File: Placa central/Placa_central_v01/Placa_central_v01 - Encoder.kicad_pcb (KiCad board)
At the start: 2 copper layers, 20 parts, among them J1 Conn_01x01_Female, J2 Conn_01x01_Female, J3 Conn_01x01_Female, J4 Conn_01x01_Female, J5 Conn_01x01_Female, J6 Conn_01x01_Female, U1 TCRT5000Esq, U2 LM741Esq, U3 TCRT5000Dir, U4 LM741

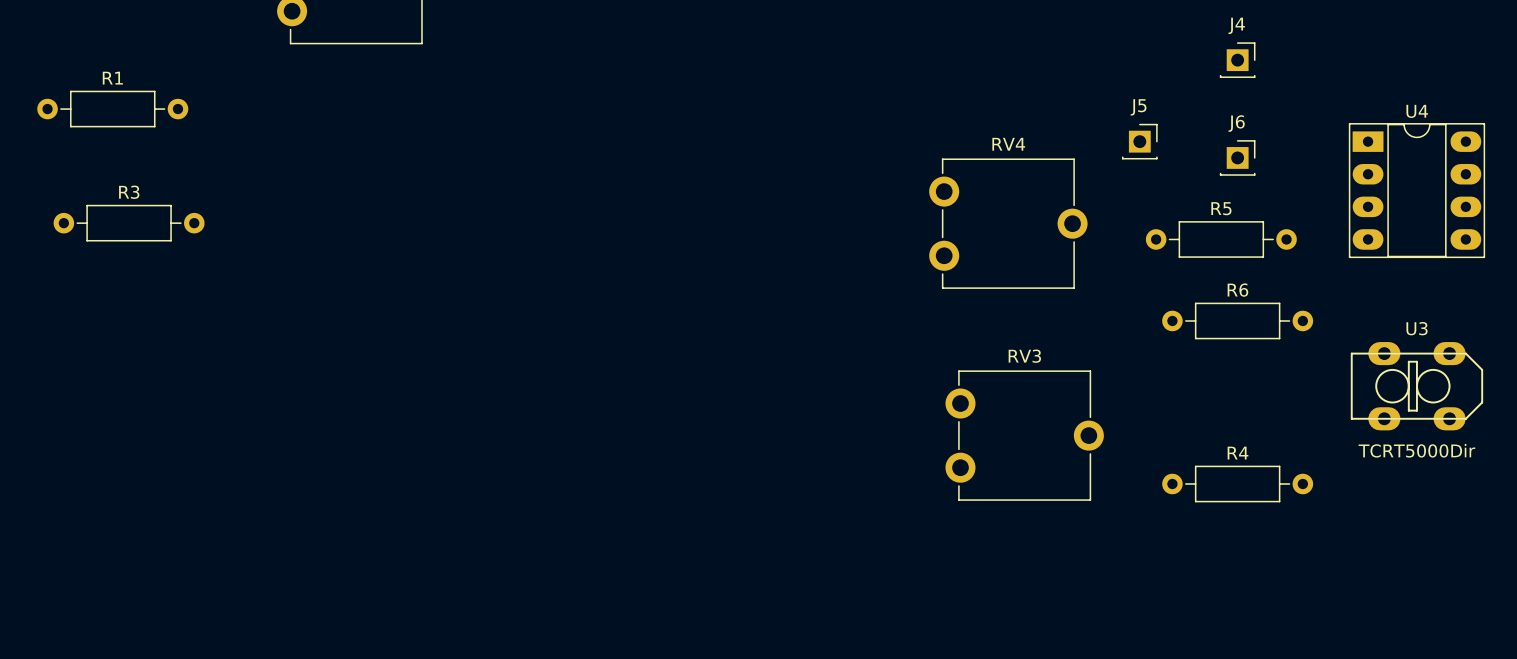
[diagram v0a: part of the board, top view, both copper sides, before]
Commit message: Adicionado Furos a placa encoder. Falta root
Adicionados os furos do suporte para o andar superior e para fixação no case do motor. Falta root
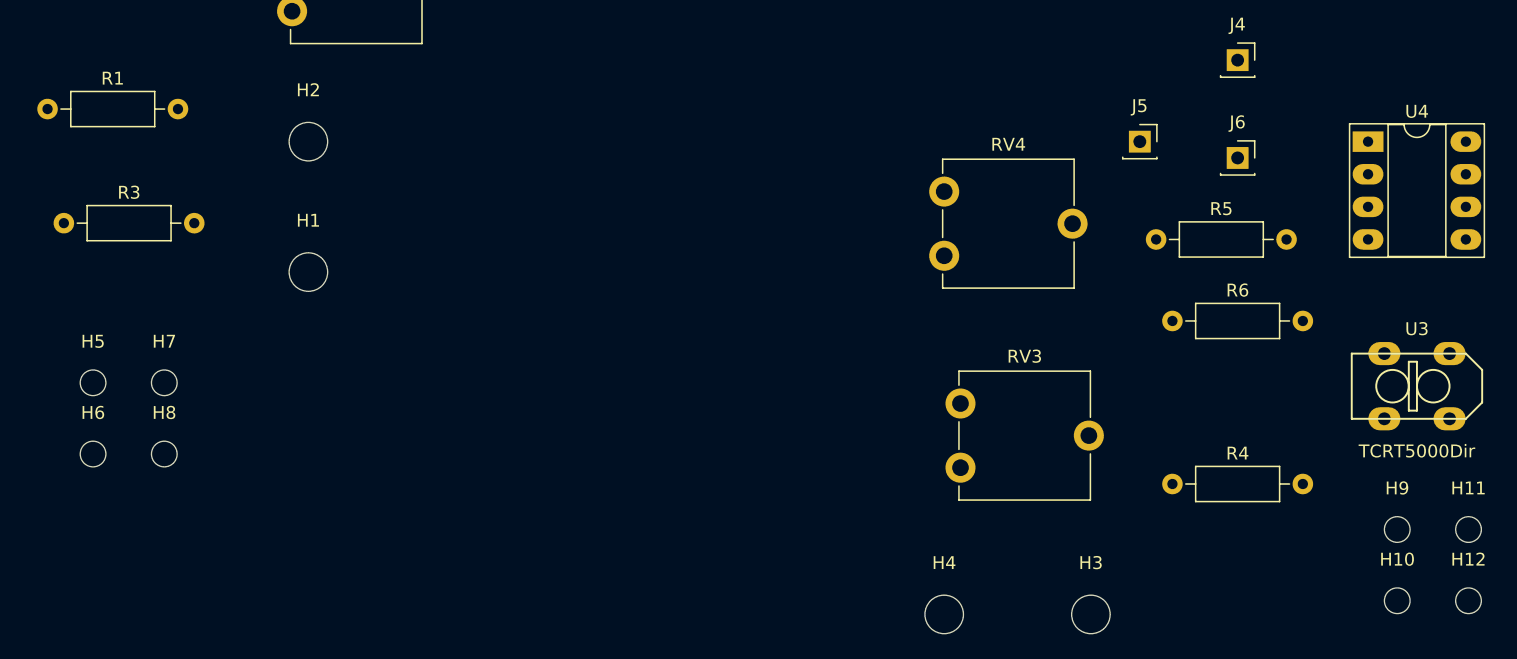
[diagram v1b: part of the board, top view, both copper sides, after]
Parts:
- added H1: Furo1Esq, MountingHole:MountingHole_3mm, F.Cu at (130.8, 110.5)
- added H10: Furo4Dir, MountingHole:MountingHole_2mm, F.Cu at (215.6, 136.1)
- added H11: Furo5Dir, MountingHole:MountingHole_2mm, F.Cu at (221.2, 130.5)
- added H12: Furo6Dir, MountingHole:MountingHole_2mm, F.Cu at (221.2, 136.1)
- added H2: Furo2Esq, MountingHole:MountingHole_3mm, F.Cu at (130.8, 100.3)
- added H3: Furo1Dir, MountingHole:MountingHole_3mm, F.Cu at (191.8, 137.2)
- added H4: Furo2Dir, MountingHole:MountingHole_3mm, F.Cu at (180.3, 137.2)
- added H5: Furo3Esq, MountingHole:MountingHole_2mm, F.Cu at (114.0, 119.1)
- added H6: Furo4Esq, MountingHole:MountingHole_2mm, F.Cu at (114.0, 124.7)
- added H7: Furo5Esq, MountingHole:MountingHole_2mm, F.Cu at (119.6, 119.1)
- added H8: Furo6Esq, MountingHole:MountingHole_2mm, F.Cu at (119.6, 124.7)
- added H9: Furo3Dir, MountingHole:MountingHole_2mm, F.Cu at (215.6, 130.5)
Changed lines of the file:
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@@
     (tracks 0)
     (zones 0)
-    (modules 20)
+    (modules 32)
     (nets 27)
   )
@@
     )
   )
+  (module MountingHole:MountingHole_3mm (layer F.Cu)
+    (at 130.81 110.49)
+    (descr "Mounting Hole 3mm, no annular")
+    (tags "mounting hole 3mm no annular")
+    (attr virtual)
+    (fp_text reference H1 (at 0 -4) (layer F.SilkS)
+      (effects (font (size 1 1) (thickness 0.15)))
+    )
+    (fp_text value Furo1Esq (at 0 4) (layer F.Fab)
+      (effects (font (size 1 1) (thickness 0.15)))
+    )
+    (fp_text user %R (at 0.3 0) (layer F.Fab)
+      (effects (font (size 1 1) (thickness 0.15)))
+    )
+    (fp_circle (center 0 0) (end 3 0) (layer Cmts.User) (width 0.15))
+    (fp_circle (center 0 0) (end 3.25 0) (layer F.CrtYd) (width 0.05))
+    (pad 1 np_thru_hole circle (at 0 0) (size 3 3) (drill 3) (layers *.Cu *.Mask))
+  )
+  (module MountingHole:MountingHole_3mm (layer F.Cu)
+    (at 130.81 100.33)
+    (descr "Mounting Hole 3mm, no annular")
+    (tags "mounting hole 3mm no annular")
+    (attr virtual)
+    (fp_text reference H2 (at 0 -4) (layer F.SilkS)
+      (effects (font (size 1 1) (thickness 0.15)))
+    )
+    (fp_text value Furo2Esq (at 0 4) (layer F.Fab)
+      (effects (font (size 1 1) (thickness 0.15)))
+    )
+    (fp_circle (center 0 0) (end 3.25 0) (layer F.CrtYd) (width 0.05))
+    (fp_circle (center 0 0) (end 3 0) (layer Cmts.User) (width 0.15))
+    (fp_text user %R (at 0.3 0) (layer F.Fab)
+      (effects (font (size 1 1) (thickness 0.15)))
+    )
+    (pad 1 np_thru_hole circle (at 0 0) (size 3 3) (drill 3) (layers *.Cu *.Mask))
+  )
+  (module MountingHole:MountingHole_3mm (layer F.Cu)
+    (at 191.77 137.16)
+    (descr "Mounting Hole 3mm, no annular")
+    (tags "mounting hole 3mm no annular")
+    (attr virtual)
+    (fp_text reference H3 (at 0 -4) (layer F.SilkS)
+      (effects (font (size 1 1) (thickness 0.15)))
+    )
+    (fp_text value Furo1Dir (at 0 4) (layer F.Fab)
+      (effects (font (size 1 1) (thickness 0.15)))
+    )
+    (fp_text user %R (at 0.3 0) (layer F.Fab)
+      (effects (font (size 1 1) (thickness 0.15)))
+    )
+    (fp_circle (center 0 0) (end 3 0) (layer Cmts.User) (width 0.15))
+    (fp_circle (center 0 0) (end 3.25 0) (layer F.CrtYd) (width 0.05))
+    (pad 1 np_thru_hole circle (at 0 0) (size 3 3) (drill 3) (layers *.Cu *.Mask))
+  )
+  (module MountingHole:MountingHole_3mm (layer F.Cu)
+    (at 180.34 137.16)
+    (descr "Mounting Hole 3mm, no annular")
+    (tags "mounting hole 3mm no annular")
+    (attr virtual)
+    (fp_text reference H4 (at 0 -4) (layer F.SilkS)
+      (effects (font (size 1 1) (thickness 0.15)))
+    )
+    (fp_text value Furo2Dir (at 0 4) (layer F.Fab)
+      (effects (font (size 1 1) (thickness 0.15)))
+    )
+    (fp_circle (center 0 0) (end 3.25 0) (layer F.CrtYd) (width 0.05))
+    (fp_circle (center 0 0) (end 3 0) (layer Cmts.User) (width 0.15))
+    (fp_text user %R (at 0.3 0) (layer F.Fab)
+      (effects (font (size 1 1) (thickness 0.15)))
+    )
+    (pad 1 np_thru_hole circle (at 0 0) (size 3 3) (drill 3) (layers *.Cu *.Mask))
+  )
+  (module MountingHole:MountingHole_2mm (layer F.Cu)
+    (at 114.035001 119.115001)
+    (descr "Mounting Hole 2mm, no annular")
+    (tags "mounting hole 2mm no annular")
+    (attr virtual)
+    (fp_text reference H5 (at 0 -3.2) (layer F.SilkS)
+      (effects (font (size 1 1) (thickness 0.15)))
+    )
+    (fp_text value Furo3Esq (at 0 3.1) (layer F.Fab)
+      (effects (font (size 1 1) (thickness 0.15)))
+    )
+    (fp_circle (center 0 0) (end 2.25 0) (layer F.CrtYd) (width 0.05))
+    (fp_circle (center 0 0) (end 2 0) (layer Cmts.User) (width 0.15))
+    (fp_text user %R (at 0.3 0) (layer F.Fab)
+      (effects (font (size 1 1) (thickness 0.15)))
+    )
+    (pad "" np_thru_hole circle (at 0 0) (size 2 2) (drill 2) (layers *.Cu *.Mask))
+  )
+  (module MountingHole:MountingHole_2mm (layer F.Cu)
+    (at 114.035001 124.665001)
+    (descr "Mounting Hole 2mm, no annular")
+    (tags "mounting hole 2mm no annular")
+    (attr virtual)
+    (fp_text reference H6 (at 0 -3.2) (layer F.SilkS)
+      (effects (font (size 1 1) (thickness 0.15)))
+    )
+    (fp_text value Furo4Esq (at 0 3.1) (layer F.Fab)
+      (effects (font (size 1 1) (thickness 0.15)))
+    )
+    (fp_text user %R (at 0.3 0) (layer F.Fab)
+      (effects (font (size 1 1) (thickness 0.15)))
+    )
+    (fp_circle (center 0 0) (end 2 0) (layer Cmts.User) (width 0.15))
+    (fp_circle (center 0 0) (end 2.25 0) (layer F.CrtYd) (width 0.05))
+    (pad "" np_thru_hole circle (at 0 0) (size 2 2) (drill 2) (layers *.Cu *.Mask))
+  )
+  (module MountingHole:MountingHole_2mm (layer F.Cu)
+    (at 119.585001 119.115001)
+    (descr "Mounting Hole 2mm, no annular")
+    (tags "mounting hole 2mm no annular")
+    (attr virtual)
+    (fp_text reference H7 (at 0 -3.2) (layer F.SilkS)
+      (effects (font (size 1 1) (thickness 0.15)))
+    )
+    (fp_text value Furo5Esq (at 0 3.1) (layer F.Fab)
+      (effects (font (size 1 1) (thickness 0.15)))
+    )
+    (fp_text user %R (at 0.3 0) (layer F.Fab)
+      (effects (font (size 1 1) (thickness 0.15)))
+    )
+    (fp_circle (center 0 0) (end 2 0) (layer Cmts.User) (width 0.15))
+    (fp_circle (center 0 0) (end 2.25 0) (layer F.CrtYd) (width 0.05))
+    (pad "" np_thru_hole circle (at 0 0) (size 2 2) (drill 2) (layers *.Cu *.Mask))
+  )
+  (module MountingHole:MountingHole_2mm (layer F.Cu)
+    (at 119.585001 124.665001)
+    (descr "Mounting Hole 2mm, no annular")
+    (tags "mounting hole 2mm no annular")
+    (attr virtual)
+    (fp_text reference H8 (at 0 -3.2) (layer F.SilkS)
+      (effects (font (size 1 1) (thickness 0.15)))
+    )
+    (fp_text value Furo6Esq (at 0 3.1) (layer F.Fab)
+      (effects (font (size 1 1) (thickness 0.15)))
+    )
+    (fp_circle (center 0 0) (end 2.25 0) (layer F.CrtYd) (width 0.05))
+    (fp_circle (center 0 0) (end 2 0) (layer Cmts.User) (width 0.15))
+    (fp_text user %R (at 0.3 0) (layer F.Fab)
+      (effects (font (size 1 1) (thickness 0.15)))
+    )
+    (pad "" np_thru_hole circle (at 0 0) (size 2 2) (drill 2) (layers *.Cu *.Mask))
+  )
+  (module MountingHole:MountingHole_2mm (layer F.Cu)
+    (at 215.635001 130.545001)
+    (descr "Mounting Hole 2mm, no annular")
+    (tags "mounting hole 2mm no annular")
+    (attr virtual)
+    (fp_text reference H9 (at 0 -3.2) (layer F.SilkS)
+      (effects (font (size 1 1) (thickness 0.15)))
+    )
+    (fp_text value Furo3Dir (at 0 3.1) (layer F.Fab)
+      (effects (font (size 1 1) (thickness 0.15)))
+    )
+    (fp_text user %R (at 0.3 0) (layer F.Fab)
+      (effects (font (size 1 1) (thickness 0.15)))
+    )
+    (fp_circle (center 0 0) (end 2 0) (layer Cmts.User) (width 0.15))
+    (fp_circle (center 0 0) (end 2.25 0) (layer F.CrtYd) (width 0.05))
+    (pad "" np_thru_hole circle (at 0 0) (size 2 2) (drill 2) (layers *.Cu *.Mask))
+  )
+  (module MountingHole:MountingHole_2mm (layer F.Cu)
+    (at 215.635001 136.095001)
+    (descr "Mounting Hole 2mm, no annular")
+    (tags "mounting hole 2mm no annular")
+    (attr virtual)
+    (fp_text reference H10 (at 0 -3.2) (layer F.SilkS)
+      (effects (font (size 1 1) (thickness 0.15)))
+    )
+    (fp_text value Furo4Dir (at 0 3.1) (layer F.Fab)
+      (effects (font (size 1 1) (thickness 0.15)))
+    )
+    (fp_text user %R (at 0.3 0) (layer F.Fab)
+      (effects (font (size 1 1) (thickness 0.15)))
+    )
+    (fp_circle (center 0 0) (end 2 0) (layer Cmts.User) (width 0.15))
+    (fp_circle (center 0 0) (end 2.25 0) (layer F.CrtYd) (width 0.05))
+    (pad "" np_thru_hole circle (at 0 0) (size 2 2) (drill 2) (layers *.Cu *.Mask))
+  )
+  (module MountingHole:MountingHole_2mm (layer F.Cu)
+    (at 221.185001 130.545001)
+    (descr "Mounting Hole 2mm, no annular")
+    (tags "mounting hole 2mm no annular")
+    (attr virtual)
+    (fp_text reference H11 (at 0 -3.2) (layer F.SilkS)
+      (effects (font (size 1 1) (thickness 0.15)))
+    )
+    (fp_text value Furo5Dir (at 0 3.1) (layer F.Fab)
+      (effects (font (size 1 1) (thickness 0.15)))
+    )
+    (fp_circle (center 0 0) (end 2.25 0) (layer F.CrtYd) (width 0.05))
+    (fp_circle (center 0 0) (end 2 0) (layer Cmts.User) (width 0.15))
+    (fp_text user %R (at 0.3 0) (layer F.Fab)
+      (effects (font (size 1 1) (thickness 0.15)))
+    )
+    (pad "" np_thru_hole circle (at 0 0) (size 2 2) (drill 2) (layers *.Cu *.Mask))
+  )
+  (module MountingHole:MountingHole_2mm (layer F.Cu)
+    (at 221.185001 136.095001)
+    (descr "Mounting Hole 2mm, no annular")
+    (tags "mounting hole 2mm no annular")
+    (attr virtual)
+    (fp_text reference H12 (at 0 -3.2) (layer F.SilkS)
+      (effects (font (size 1 1) (thickness 0.15)))
+    )
+    (fp_text value Furo6Dir (at 0 3.1) (layer F.Fab)
+      (effects (font (size 1 1) (thickness 0.15)))
+    )
+    (fp_circle (center 0 0) (end 2.25 0) (layer F.CrtYd) (width 0.05))
+    (fp_circle (center 0 0) (end 2 0) (layer Cmts.User) (width 0.15))
+    (fp_text user %R (at 0.3 0) (layer F.Fab)
+      (effects (font (size 1 1) (thickness 0.15)))
+    )
+    (pad "" np_thru_hole circle (at 0 0) (size 2 2) (drill 2) (layers *.Cu *.Mask))
+  )
 )

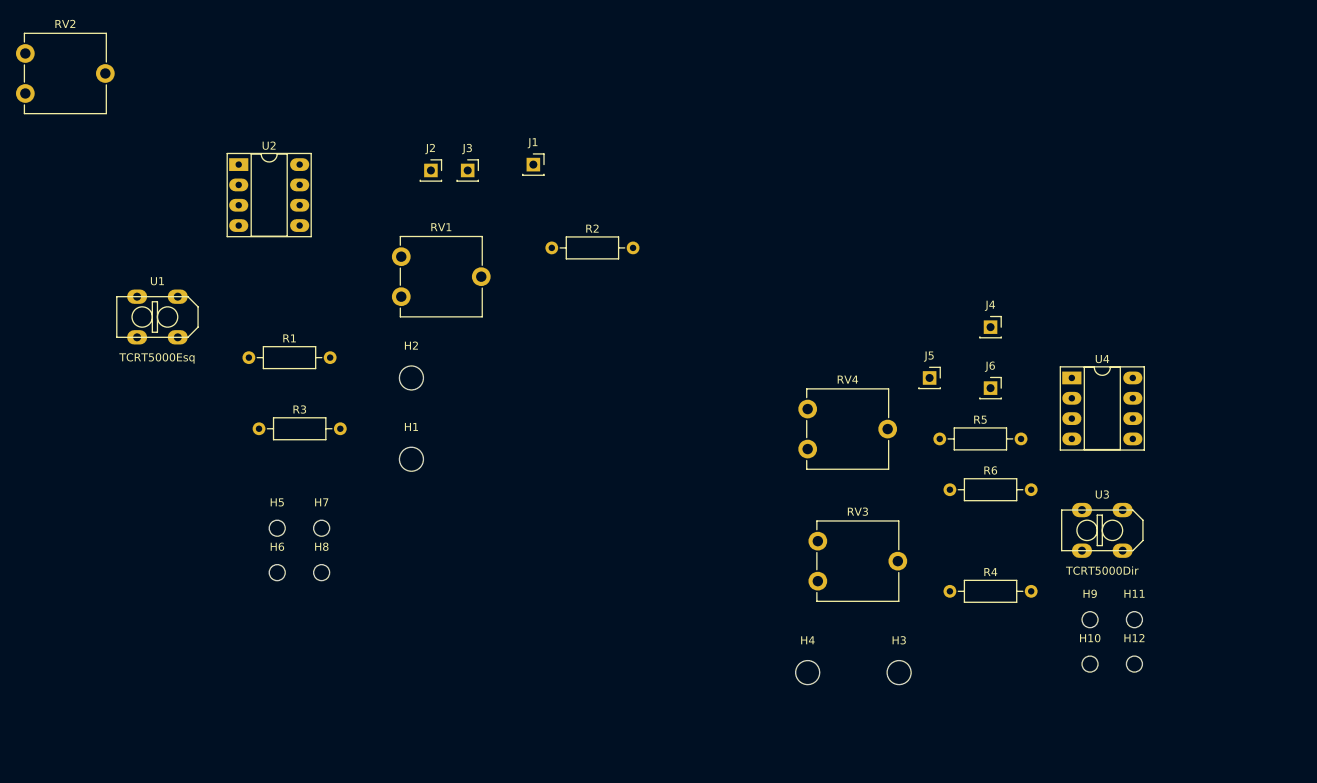
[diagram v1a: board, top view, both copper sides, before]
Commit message: Tentativa de root placa de encoder
placa da direita rooteada e a placa da esquerda em processo.
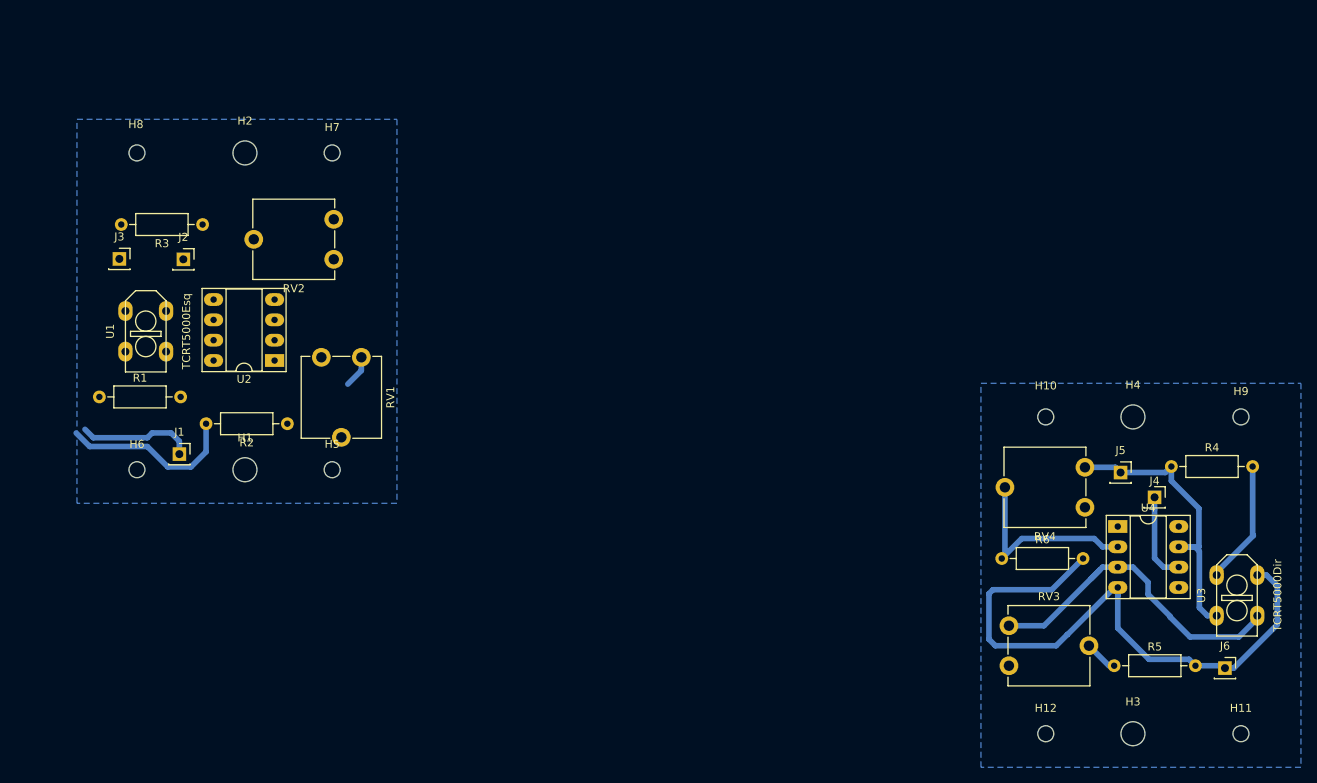
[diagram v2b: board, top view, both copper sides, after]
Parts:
- moved H8 57.3 mm to (96.5, 72.2)
- moved J1 57.2 mm to (101.8, 109.8)
- moved H4 51.7 mm to (221.0, 105.2)
- moved H7 46.9 mm to (120.9, 72.2)
- moved J6 45.6 mm to (232.5, 136.6)
- moved J3 44.9 mm to (94.3, 85.5)
- moved RV2 41.6 mm to (121.1, 80.5), turned to 180 degrees
- moved R2 39.7 mm to (115.3, 106.0), turned to 180 degrees
- moved R5 35.8 mm to (218.7, 136.3)
- moved H2 35.0 mm to (110.0, 72.2)
- moved RV4 34.7 mm to (215.0, 111.5), turned to 180 degrees
- moved J2 32.9 mm to (102.3, 85.5)
- moved R4 31.8 mm to (225.8, 111.4)
- moved H9 31.6 mm to (234.5, 105.2)
- moved H10 31.4 mm to (210.1, 105.2)
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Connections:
- J5 pad 1: Vcc -> VccDir
- J6 pad 1: GND -> GNDDir
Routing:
- net GNDDir: track 0.00 -> 77.0 mm
- net Net-(RV3-Pad3): track 0.00 -> 41.9 mm
- net VccDir: track 0.00 -> 37.4 mm
- net Net-(R6-Pad1): track 0.00 -> 25.0 mm
- net GNDEsq: track 0.00 -> 23.3 mm
- net Net-(R4-Pad2): track 0.00 -> 15.5 mm
- net SinalEncoderEsq: track 0.00 -> 14.5 mm
- net SinalEncoderDIr: track 0.00 -> 11.1 mm
- net Net-(RV1-Pad3): track 0.00 -> 4.45 mm
- net Net-(R5-Pad1): track 0.00 -> 4.19 mm
- net VccEsq: track 0.00 -> 0.80 mm
- added copper zone on B.Cu, net (none)
- added copper zone on B.Cu, net GNDDir
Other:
- net class Default: clearance 0.2 -> 0.4; trace_width 0.25 -> 0.7
- rule trace_clearance: 0.2 -> 0.4

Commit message: Finalização do roteamento PCB Encoder
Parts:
- moved R3 79.7 mm to (178.0, 112.5), turned to 270 degrees
- moved R1 75.0 mm to (159.0, 136.0), turned to 180 degrees
- moved R2 71.8 mm to (184.0, 127.0), turned to 90 degrees
- moved RV1 66.7 mm to (173.5, 137.0), turned to 0 degrees
- moved J3 66.3 mm to (151.5, 119.0)
- moved H1 65.9 mm to (167.4, 144.2)
- moved H5 65.9 mm to (178.3, 144.2)
- moved H6 65.9 mm to (153.9, 144.2)
- moved U1 65.9 mm to (155.1, 126.8)
- moved H2 65.9 mm to (167.4, 104.5)
- moved H7 65.9 mm to (178.3, 104.5)
- moved H8 65.9 mm to (153.9, 104.5)
- moved U2 64.2 mm to (169.5, 130.0)
- moved J2 61.5 mm to (156.5, 114.5)
- moved J1 56.0 mm to (157.0, 119.0)
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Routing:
- net VccEsq: track 0.80 -> 70.9 mm
- net GNDEsq: track 23.3 -> 68.8 mm
- net Net-(RV1-Pad3): track 4.45 -> 30.0 mm
- net Net-(R3-Pad1): track 0.00 -> 25.1 mm
- net Net-(R1-Pad2): track 0.00 -> 13.2 mm
- net Net-(R2-Pad1): track 0.00 -> 7.71 mm
- net SinalEncoderEsq: track 14.5 -> 8.24 mm
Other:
- board text added: "*"
- board text added: "+"
- board text added: "-"
